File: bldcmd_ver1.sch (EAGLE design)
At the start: 62 parts, among them IC1 STSPIN32F0, IC2 AS5047P-ATSM, IC3 ADM4852ACPZ-REEL7, J1 DF65-3P-1.7V(21), Q1 PSMN2R4-30MLD, Q2 PSMN2R4-30MLD, Q3 PSMN2R4-30MLD, Q4 PSMN2R4-30MLD, Q5 PSMN2R4-30MLD, Q6 PSMN2R4-30MLD

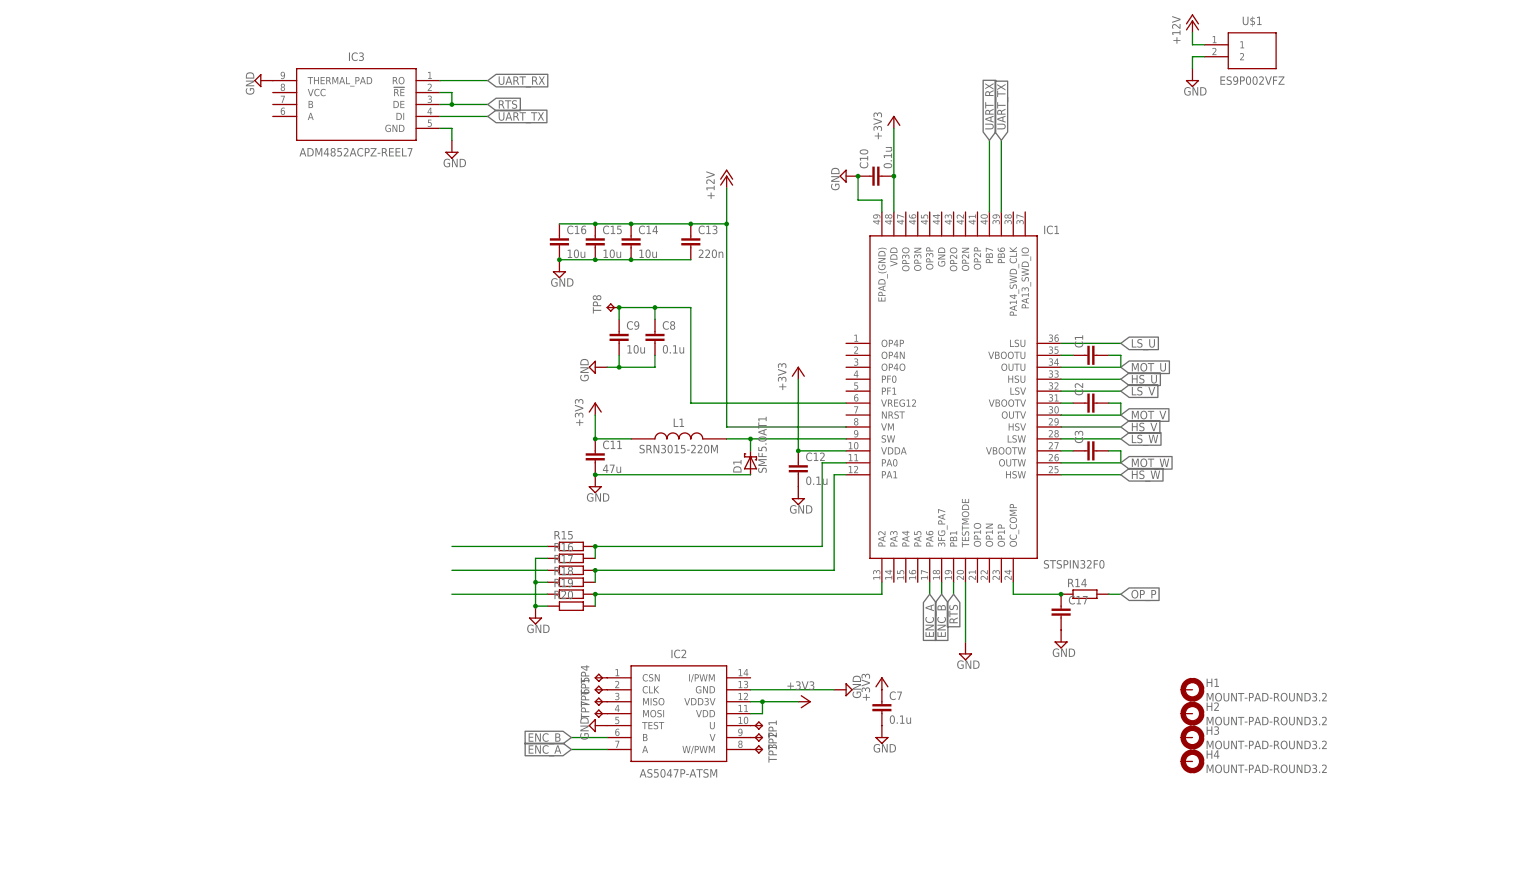
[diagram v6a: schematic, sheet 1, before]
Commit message: オペアンプつけた
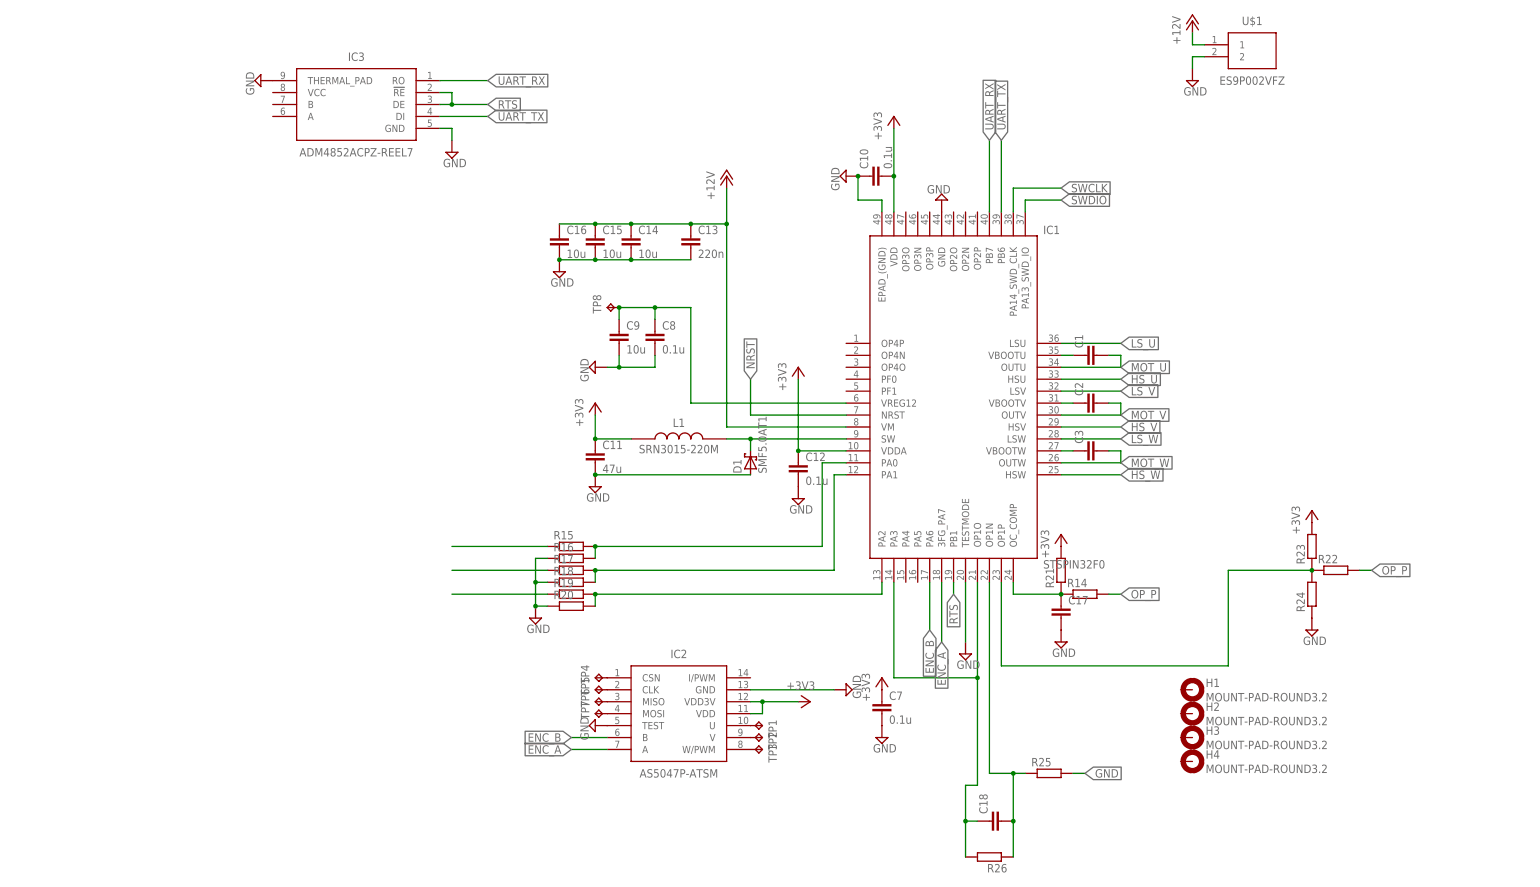
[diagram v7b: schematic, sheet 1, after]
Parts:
- added C18: (no value), rcl:C-EUC0402
- added R21, R22, R23, R24, R25, R26: (no value), rcl:R-EU_R0402
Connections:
- new net N$26: IC1.OP1P, R22.1, R23.1, R24.2
- new net N$27: C18.2, IC1.OP1N, R25.1, R26.1
- new net N$28: C18.1, IC1.OP1O, IC1.PA3, R26.2
- new net NRST: IC1.NRST
- new net SWCLK: IC1.PA14_SWD_CLK
- new net SWDIO: IC1.PA13_SWD_IO
- net +3V3: now also R21.2, R23.2
- net ENC_A: now also IC1.3FG_PA7; no longer IC1.PA6
- net ENC_B: now also IC1.PA6; no longer IC1.3FG_PA7
- net GND: now also IC1.GND, R24.1, R25.2
- net N$10: now also R21.1
- net OP_P: now also R22.2
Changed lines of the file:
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@@
 <part name="R20" library="rcl" library_urn="urn:adsk.eagle:library:334" deviceset="R-EU_" device="R0402" package3d_urn="urn:adsk.eagle:package:23547/1"/>
 <part name="SUPPLY15" library="supply2" library_urn="urn:adsk.eagle:library:372" deviceset="GND" device=""/>
+<part name="R21" library="rcl" library_urn="urn:adsk.eagle:library:334" deviceset="R-EU_" device="R0402" package3d_urn="urn:adsk.eagle:package:23547/1"/>
+<part name="+3V6" library="supply1" library_urn="urn:adsk.eagle:library:371" deviceset="+3V3" device=""/>
+<part name="R22" library="rcl" library_urn="urn:adsk.eagle:library:334" deviceset="R-EU_" device="R0402" package3d_urn="urn:adsk.eagle:package:23547/1"/>
+<part name="R23" library="rcl" library_urn="urn:adsk.eagle:library:334" deviceset="R-EU_" device="R0402" package3d_urn="urn:adsk.eagle:package:23547/1"/>
+<part name="R24" library="rcl" library_urn="urn:adsk.eagle:library:334" deviceset="R-EU_" device="R0402" package3d_urn="urn:adsk.eagle:package:23547/1"/>
+<part name="R25" library="rcl" library_urn="urn:adsk.eagle:library:334" deviceset="R-EU_" device="R0402" package3d_urn="urn:adsk.eagle:package:23547/1"/>
+<part name="C18" library="rcl" library_urn="urn:adsk.eagle:library:334" deviceset="C-EU" device="C0402" package3d_urn="urn:adsk.eagle:package:23626/1"/>
+<part name="R26" library="rcl" library_urn="urn:adsk.eagle:library:334" deviceset="R-EU_" device="R0402" package3d_urn="urn:adsk.eagle:package:23547/1"/>
+<part name="SUPPLY16" library="supply2" library_urn="urn:adsk.eagle:library:372" deviceset="GND" device=""/>
+<part name="+3V7" library="supply1" library_urn="urn:adsk.eagle:library:371" deviceset="+3V3" device=""/>
+<part name="SUPPLY17" library="supply2" library_urn="urn:adsk.eagle:library:372" deviceset="GND" device=""/>
 </parts>
 <sheets>
@@
 <instance part="R20" gate="G$1" x="-50.8" y="-55.88"/>
 <instance part="SUPPLY15" gate="GND" x="-58.42" y="-58.42"/>
+<instance part="R21" gate="G$1" x="53.34" y="-48.26" rot="R90"/>
+<instance part="+3V6" gate="G$1" x="53.34" y="-40.64"/>
+<instance part="R22" gate="G$1" x="111.76" y="-48.26"/>
+<instance part="R23" gate="G$1" x="106.68" y="-43.18" rot="R90"/>
+<instance part="R24" gate="G$1" x="106.68" y="-53.34" rot="R90"/>
+<instance part="R25" gate="G$1" x="50.8" y="-91.44"/>
+<instance part="C18" gate="G$1" x="38.1" y="-101.6" rot="R90"/>
+<instance part="R26" gate="G$1" x="38.1" y="-109.22" rot="R180"/>
+<instance part="SUPPLY16" gate="GND" x="106.68" y="-60.96"/>
+<instance part="+3V7" gate="G$1" x="106.68" y="-35.56"/>
+<instance part="SUPPLY17" gate="GND" x="27.94" y="30.48" rot="R180"/>
 </instances>
 <busses>
@@
 <junction x="-58.42" y="-55.88"/>
 </segment>
+<segment>
+<pinref part="R25" gate="G$1" pin="2"/>
+<wire x1="55.88" y1="-91.44" x2="58.42" y2="-91.44" width="0.1524" layer="91"/>
+<label x="58.42" y="-91.44" size="1.778" layer="95" xref="yes"/>
+</segment>
+<segment>
+<pinref part="R24" gate="G$1" pin="1"/>
+<pinref part="SUPPLY16" gate="GND" pin="GND"/>
+</segment>
+<segment>
+<pinref part="IC1" gate="G$1" pin="GND"/>
+<pinref part="SUPPLY17" gate="GND" pin="GND"/>
+</segment>
 </net>
 <net name="+3V3" class="0">
@@
 <junction x="-2.54" y="-22.86"/>
 </segment>
+<segment>
+<pinref part="R21" gate="G$1" pin="2"/>
+<pinref part="+3V6" gate="G$1" pin="+3V3"/>
+</segment>
+<segment>
+<pinref part="R23" gate="G$1" pin="2"/>
+<pinref part="+3V7" gate="G$1" pin="+3V3"/>
+</segment>
 </net>
 <net name="ENC_B" class="0">
@@
 </segment>
 <segment>
-<pinref part="IC1" gate="G$1" pin="3FG_PA7"/>
-<wire x1="27.94" y1="-50.8" x2="27.94" y2="-53.34" width="0.1524" layer="91"/>
-<label x="27.94" y="-53.34" size="1.778" layer="95" rot="R270" xref="yes"/>
+<pinref part="IC1" gate="G$1" pin="PA6"/>
+<wire x1="25.4" y1="-50.8" x2="25.4" y2="-60.96" width="0.1524" layer="91"/>
+<label x="25.4" y="-60.96" size="1.778" layer="95" rot="R270" xref="yes"/>
 </segment>
 </net>
@@
 </segment>
 <segment>
-<pinref part="IC1" gate="G$1" pin="PA6"/>
-<wire x1="25.4" y1="-50.8" x2="25.4" y2="-53.34" width="0.1524" layer="91"/>
-<label x="25.4" y="-53.34" size="1.778" layer="95" rot="R270" xref="yes"/>
+<pinref part="IC1" gate="G$1" pin="3FG_PA7"/>
+<wire x1="27.94" y1="-50.8" x2="27.94" y2="-63.5" width="0.1524" layer="91"/>
+<label x="27.94" y="-63.5" size="1.778" layer="95" rot="R270" xref="yes"/>
 </segment>
 </net>
@@
 <wire x1="43.18" y1="-53.34" x2="53.34" y2="-53.34" width="0.1524" layer="91"/>
 <junction x="53.34" y="-53.34"/>
+<pinref part="R21" gate="G$1" pin="1"/>
 </segment>
 </net>
@@
 <wire x1="63.5" y1="-53.34" x2="66.04" y2="-53.34" width="0.1524" layer="91"/>
 <label x="66.04" y="-53.34" size="1.778" layer="95" xref="yes"/>
+</segment>
+<segment>
+<pinref part="R22" gate="G$1" pin="2"/>
+<wire x1="116.84" y1="-48.26" x2="119.38" y2="-48.26" width="0.1524" layer="91"/>
+<label x="119.38" y="-48.26" size="1.778" layer="95" xref="yes"/>
 </segment>
 </net>
@@
 </segment>
 </net>
+<net name="N$26" class="0">
+<segment>
+<pinref part="R22" gate="G$1" pin="1"/>
+<pinref part="R23" gate="G$1" pin="1"/>
+<pinref part="R24" gate="G$1" pin="2"/>
+<junction x="106.68" y="-48.26"/>
+<pinref part="R24" gate="G$1" pin="2"/>
+<wire x1="106.68" y1="-48.26" x2="88.9" y2="-48.26" width="0.1524" layer="91"/>
+<wire x1="88.9" y1="-48.26" x2="88.9" y2="-68.58" width="0.1524" layer="91"/>
+<pinref part="IC1" gate="G$1" pin="OP1P"/>
+<wire x1="88.9" y1="-68.58" x2="40.64" y2="-68.58" width="0.1524" layer="91"/>
+<wire x1="40.64" y1="-68.58" x2="40.64" y2="-50.8" width="0.1524" layer="91"/>
+</segment>
+</net>
+<net name="N$27" class="0">
+<segment>
+<pinref part="R25" gate="G$1" pin="1"/>
+<pinref part="IC1" gate="G$1" pin="OP1N"/>
+<wire x1="45.72" y1="-91.44" x2="43.18" y2="-91.44" width="0.1524" layer="91"/>
+<wire x1="43.18" y1="-91.44" x2="38.1" y2="-91.44" width="0.1524" layer="91"/>
+<wire x1="38.1" y1="-91.44" x2="38.1" y2="-50.8" width="0.1524" layer="91"/>
+<pinref part="C18" gate="G$1" pin="2"/>
+<wire x1="43.18" y1="-101.6" x2="43.18" y2="-91.44" width="0.1524" layer="91"/>
+<junction x="43.18" y="-91.44"/>
+<pinref part="R26" gate="G$1" pin="1"/>
+<wire x1="43.18" y1="-101.6" x2="43.18" y2="-109.22" width="0.1524" layer="91"/>
+<junction x="43.18" y="-101.6"/>
+</segment>
+</net>
+<net name="N$28" class="0">
+<segment>
+<pinref part="R26" gate="G$1" pin="2"/>
+<wire x1="33.02" y1="-109.22" x2="33.02" y2="-101.6" width="0.1524" layer="91"/>
+<pinref part="C18" gate="G$1" pin="1"/>
+<wire x1="33.02" y1="-101.6" x2="35.56" y2="-101.6" width="0.1524" layer="91"/>
+<pinref part="IC1" gate="G$1" pin="OP1O"/>
+<wire x1="35.56" y1="-50.8" x2="35.56" y2="-71.12" width="0.1524" layer="91"/>
+<wire x1="35.56" y1="-71.12" x2="35.56" y2="-93.98" width="0.1524" layer="91"/>
+<wire x1="35.56" y1="-93.98" x2="33.02" y2="-93.98" width="0.1524" layer="91"/>
+<wire x1="33.02" y1="-93.98" x2="33.02" y2="-101.6" width="0.1524" layer="91"/>
+<junction x="33.02" y="-101.6"/>
+<pinref part="IC1" gate="G$1" pin="PA3"/>
+<wire x1="35.56" y1="-71.12" x2="17.78" y2="-71.12" width="0.1524" layer="91"/>
+<wire x1="17.78" y1="-71.12" x2="17.78" y2="-50.8" width="0.1524" layer="91"/>
+<junction x="35.56" y="-71.12"/>
+</segment>
+</net>
+<net name="NRST" class="0">
+<segment>
+<pinref part="IC1" gate="G$1" pin="NRST"/>
+<wire x1="7.62" y1="-15.24" x2="-12.7" y2="-15.24" width="0.1524" layer="91"/>
+<wire x1="-12.7" y1="-15.24" x2="-12.7" y2="-7.62" width="0.1524" layer="91"/>
+<label x="-12.7" y="-7.62" size="1.778" layer="95" rot="R90" xref="yes"/>
+</segment>
+</net>
+<net name="SWDIO" class="0">
+<segment>
+<pinref part="IC1" gate="G$1" pin="PA13_SWD_IO"/>
+<wire x1="45.72" y1="27.94" x2="45.72" y2="30.48" width="0.1524" layer="91"/>
+<wire x1="45.72" y1="30.48" x2="53.34" y2="30.48" width="0.1524" layer="91"/>
+<label x="53.34" y="30.48" size="1.778" layer="95" xref="yes"/>
+</segment>
+</net>
+<net name="SWCLK" class="0">
+<segment>
+<pinref part="IC1" gate="G$1" pin="PA14_SWD_CLK"/>
+<wire x1="43.18" y1="27.94" x2="43.18" y2="33.02" width="0.1524" layer="91"/>
+<wire x1="43.18" y1="33.02" x2="53.34" y2="33.02" width="0.1524" layer="91"/>
+<label x="53.34" y="33.02" size="1.778" layer="95" xref="yes"/>
+</segment>
+</net>

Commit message: 5Vレギュレータと電源LED追加
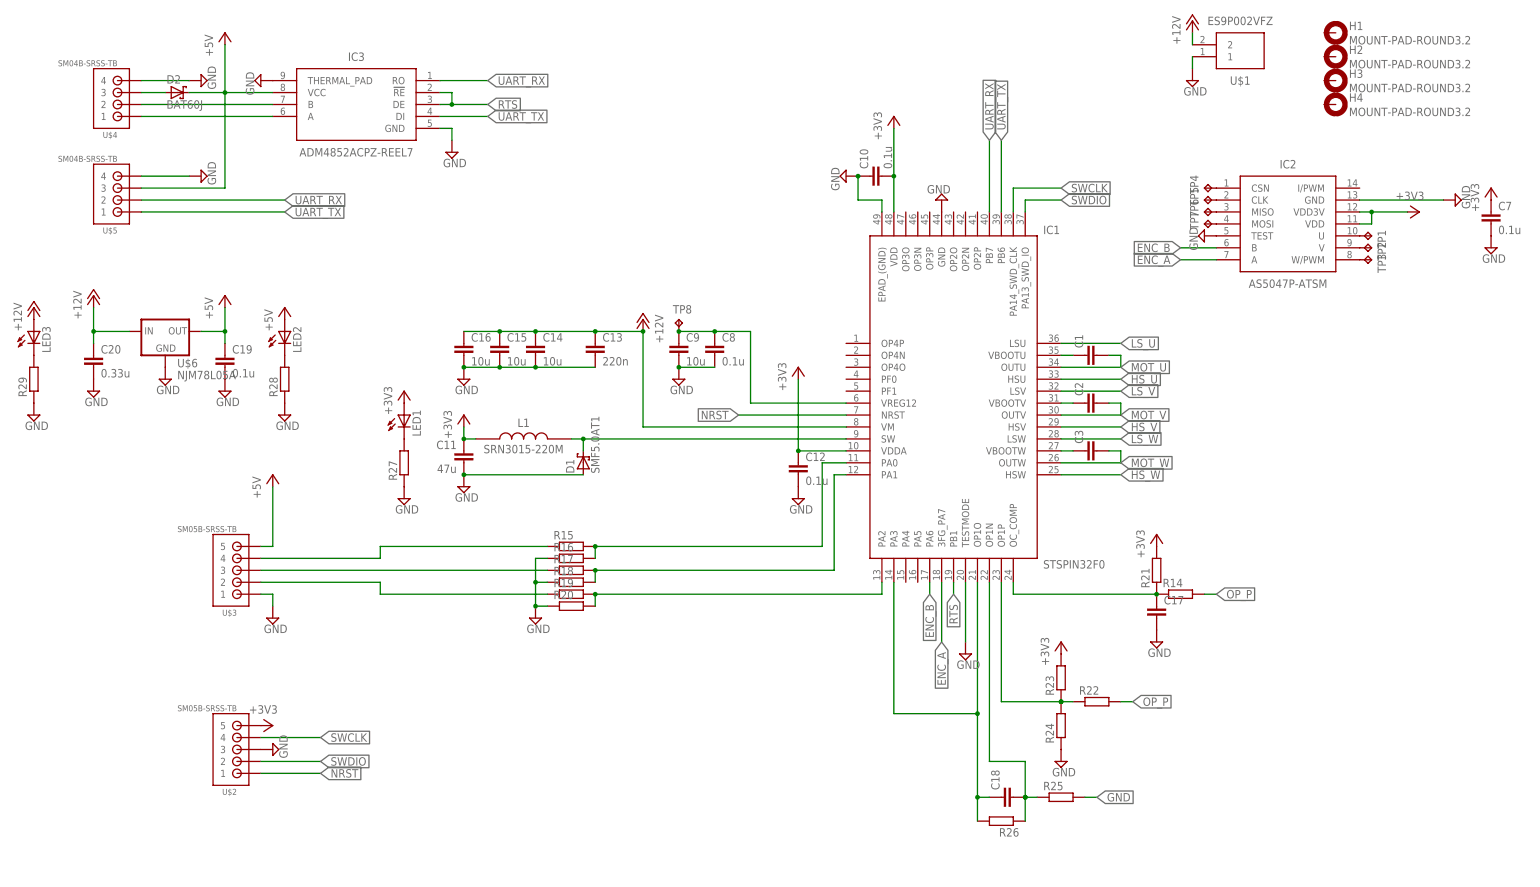
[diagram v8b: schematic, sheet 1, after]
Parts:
- added C19: 0.1u, rcl:C-EUC0603K
- added C20: 0.33u, rcl:C-EUC0805K
- added D2: BAT60J, diode:BAT60J
- added LED1, LED2, LED3: (no value), led:LEDSML0603
- added R27, R28, R29: (no value), rcl:R-EU_R0603
- added U$2, U$3: SM05B-SRSS-TB, JST-SH:SM05B-SRSS-TB
- added U$4, U$5: SM04B-SRSS-TB, JST-SH:SM04B-SRSS-TB
- added U$6: NJM78L05A, rcssl_lib:NJM78L05A
- TP8: value TPPAD1-13 -> TPB1,27; device testpad:TPPAD1-13 -> testpad:TPB1,27
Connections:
- new net +5V: C19.1, D2.C, IC3.VCC, LED2.A, U$3.5, U$5.3, U$6.OUT
- new net N$29: IC3.B, U$4.2
- new net N$30: D2.A, U$4.3
- new net N$31: LED1.C, R27.2
- new net N$32: IC3.A, U$4.1
- new net N$33: LED2.C, R28.2
- new net N$34: LED3.C, R29.2
- net +12V: now also C20.1, LED3.A, U$1.2, U$6.IN; no longer U$1.1
- net +3V3: now also LED1.A, U$2.5
- net GND: now also C19.2, C20.2, R27.1, R28.1, R29.1, U$1.1, U$2.3, U$3.1, U$4.4, U$5.4, U$6.GND; no longer U$1.2
- net N$23: now also U$3.2
- net N$24: now also U$3.3
- net N$25: now also U$3.4
- net NRST: now also U$2.1
- net SWCLK: now also U$2.4
- net SWDIO: now also U$2.2
- net UART_RX: now also U$5.2
- net UART_TX: now also U$5.1
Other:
- moved on the sheet: C11, C13, C14, C15, C16, C17, C18, C7, C8, C9, D1, H1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
